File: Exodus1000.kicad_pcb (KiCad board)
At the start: 4 copper layers, 129.5 x 63.5 mm, 78 parts, among them J1 ARJ-169, J2 USB_B_Mini, J3 Conn_01x02, M1 ET60S-02-24-02-X-VP-GP, M2 ET60S-02-24-02-X-VP-GP, M3 ET60S-02-24-02-X-VP-GP, M4 ET60S-02-24-02-X-VP-GP, U1 TM4C1294NCPDTGOOD, U2 93LCxxB, U3 FT232H, U4 tusb2077a, U5 IS42S16400J-xT, Y1 Crystal_GND24, Y2 Crystal_GND24, Y3 Crystal_GND24

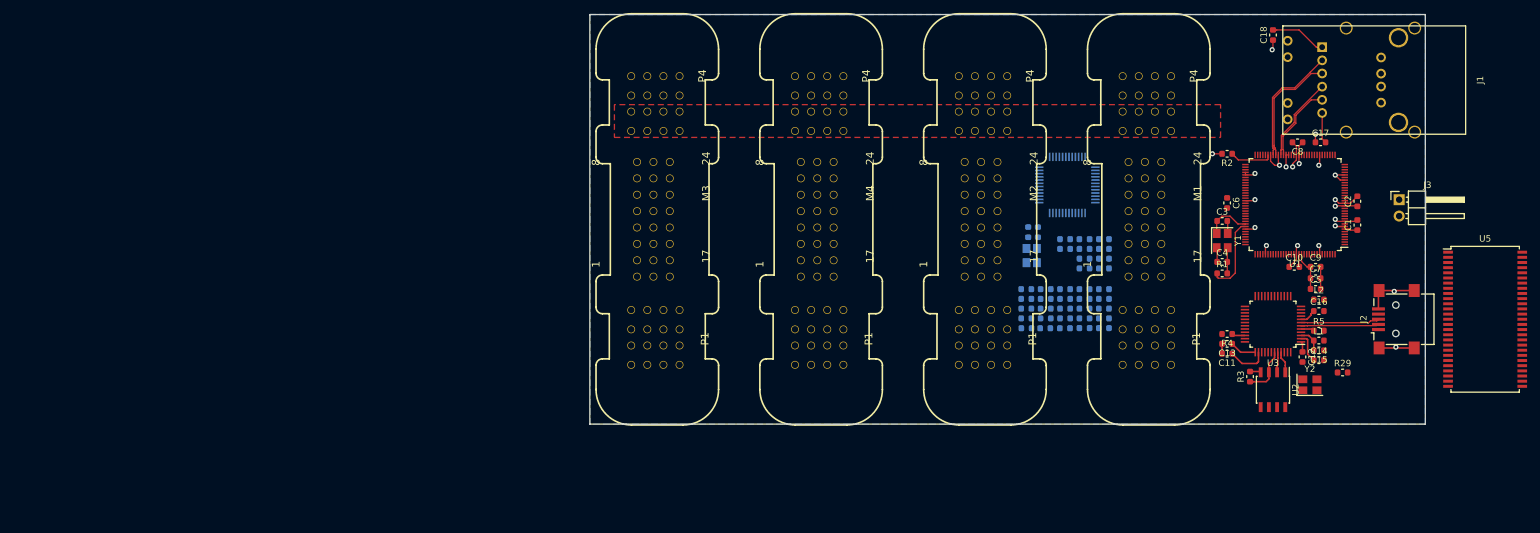
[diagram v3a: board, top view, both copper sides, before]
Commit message: schematics for expansion slots and memory
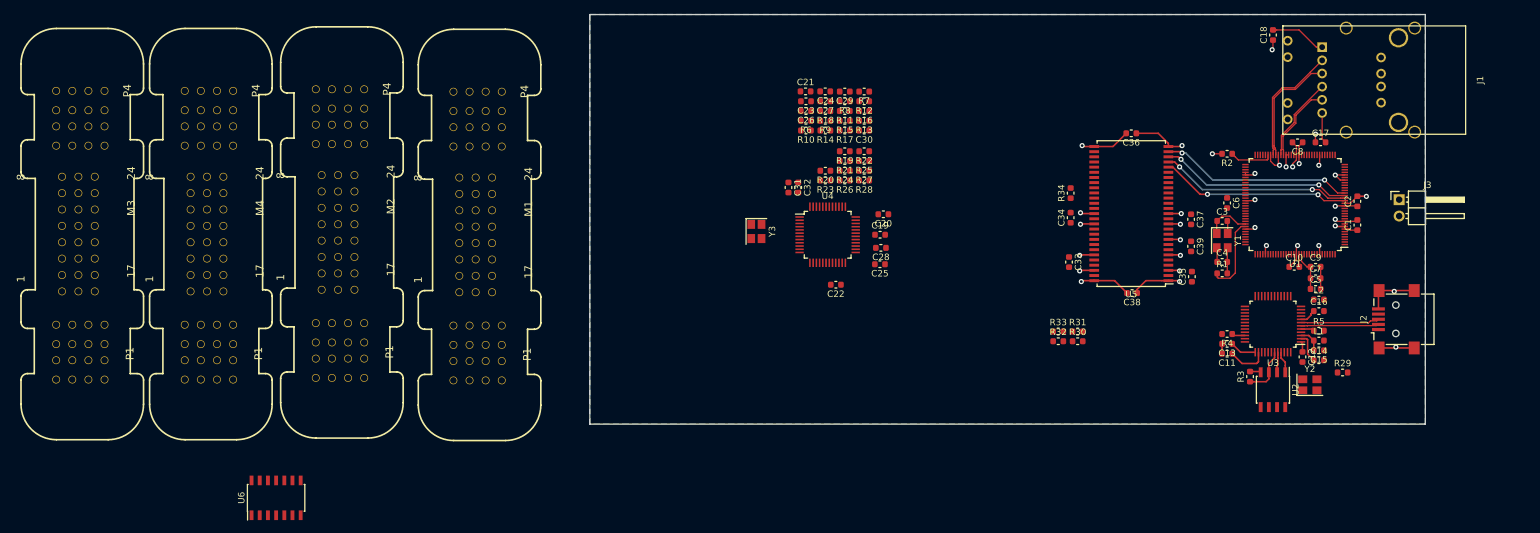
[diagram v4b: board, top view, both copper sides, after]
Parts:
- added C33: C_Small, Capacitor_SMD:C_0603_1608Metric, F.Cu at (134.0, 104.7)
- added C34: C_Small, Capacitor_SMD:C_0603_1608Metric, F.Cu at (134.2, 97.8)
- added C35: C_Small, Capacitor_SMD:C_0603_1608Metric, F.Cu at (153.0, 106.9)
- added C36: C_Small, Capacitor_SMD:C_0603_1608Metric, F.Cu at (143.6, 84.7)
- added C37: C_Small, Capacitor_SMD:C_0603_1608Metric, F.Cu at (152.9, 98.0)
- added C38: C_Small, Capacitor_SMD:C_0603_1608Metric, F.Cu at (143.8, 109.5)
- added C39: C_Small, Capacitor_SMD:C_0603_1608Metric, F.Cu at (152.9, 102.2)
- added R30: R_Small, Resistor_SMD:R_0603_1608Metric, F.Cu at (135.3, 116.9)
- added R31: R_Small, Resistor_SMD:R_0603_1608Metric, F.Cu at (135.3, 115.4)
- added R32: R_Small, Resistor_SMD:R_0603_1608Metric, F.Cu at (132.3, 116.9)
- added R33: R_Small, Resistor_SMD:R_0603_1608Metric, F.Cu at (132.3, 115.4)
- added R34: 0, Resistor_SMD:R_0603_1608Metric, F.Cu at (134.2, 94.0)
- added U6: 74LS125, Package_SO:SOIC-14_3.9x8.7mm_P1.27mm, F.Cu at (11.0, 141.2)
- C19, C20, C21, C22, C23, C24, C25, C26, C27, C28, C29, C30, C31, C32, R10, R11, R12, R13, R14, R15, R16, R17, R18, R19, R20, R21, R22, R23, R24, R25, R26, R27, R28, R6, R7, R8, R9, U4, Y3: moved to F.Cu
- U5: value IS42S16400J-xT -> IS42S16400J-xC
- moved M1 103.8 mm to (42.3, 100.5)
- moved M2 99.7 mm to (21.0, 100.1)
- moved M4 94.6 mm to (0.64, 100.3)
- moved M3 89.2 mm to (-19.3, 100.3)
- moved U5 57.3 mm to (143.6, 97.2), turned to 180 degrees
- moved C21 52.3 mm to (93.1, 78.2)
- moved C24 52.3 mm to (96.2, 78.2)
- moved R7 52.2 mm to (102.2, 78.2)
- moved C29 52.2 mm to (99.2, 78.2)
- moved C23 50.1 mm to (93.2, 79.7)
- moved R12 50.1 mm to (102.2, 79.7)
- moved C27 50.1 mm to (96.2, 79.7)
- moved R8 50.1 mm to (99.2, 79.7)
- moved C26 48.2 mm to (93.2, 81.3)
- moved R16 48.2 mm to (102.2, 81.3)
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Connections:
- net Net-(M3-Pad4) renamed /Connectors/JTAG_TD0
- C21 pad 1: Net-(C21-Pad1) -> /Connectors/sheet5C922FED/DP3
- C22 pad 1: Net-(C22-Pad1) -> /Connectors/sheet5C922FED/DM3
- C23 pad 1: Net-(C23-Pad1) -> /Connectors/sheet5C922FED/DP1
- C24 pad 1: Net-(C24-Pad1) -> /Connectors/sheet5C922FED/DM1
- C25 pad 1: Net-(C25-Pad1) -> /Connectors/sheet5C922FED/DP4
- C26 pad 1: Net-(C26-Pad1) -> /Connectors/sheet5C922FED/DM4
- C27 pad 1: Net-(C27-Pad1) -> /Connectors/sheet5C922FED/DP2
- C28 pad 1: Net-(C28-Pad1) -> /Connectors/sheet5C922FED/DP5
- C29 pad 1: Net-(C29-Pad1) -> /Connectors/sheet5C922FED/DM2
- C30 pad 1: Net-(C30-Pad1) -> /Connectors/sheet5C922FED/DM5
- J1 pad U2: Net-(J1-PadU2) -> /Connectors/D5_N
- J1 pad U3: Net-(J1-PadU3) -> /Connectors/D5_P
- M1 pad 1: Net-(M1-Pad1) -> /Connectors/D4_P
- M1 pad 10: Net-(M1-Pad10) -> /Connectors/BOARD_SENSE_4
- M1 pad 11: Net-(M1-Pad11) -> /Connectors/~SYSRESET
- M1 pad 2: Net-(M1-Pad2) -> /Connectors/D4_N
- M1 pad 3: Net-(M1-Pad3) -> /JTAG_TMS
- M1 pad 4: Net-(M1-Pad4) -> /Connectors/JTAG_TDO_3
- M1 pad 5: Net-(M1-Pad5) -> /JTAG_TDI
- M1 pad 6: Net-(M1-Pad6) -> /JTAG_TCK
- M1 pad 7: Net-(M1-Pad7) -> /Connectors/~JTAG_TRST
- M1 pad 8: Net-(M1-Pad8) -> /Connectors/~ENABLE
- M1 pad 9: Net-(M1-Pad9) -> /Connectors/~INHIBIT
- M2 pad 1: Net-(M2-Pad1) -> /Connectors/D3_P
- M2 pad 10: Net-(M2-Pad10) -> /Connectors/BOARD_SENSE_3
- M2 pad 11: Net-(M2-Pad11) -> /Connectors/~SYSRESET
- M2 pad 2: Net-(M2-Pad2) -> /Connectors/D3_N
- M2 pad 3: Net-(M2-Pad3) -> /JTAG_TMS
- M2 pad 4: Net-(M2-Pad4) -> /Connectors/JTAG_TDO_2
- M2 pad 5: Net-(M2-Pad5) -> /Connectors/JTAG_TDO_3
- M2 pad 6: Net-(M2-Pad6) -> /JTAG_TCK
- M2 pad 7: Net-(M2-Pad7) -> /Connectors/~JTAG_TRST
- M2 pad 8: Net-(M2-Pad8) -> /Connectors/~ENABLE
- M2 pad 9: Net-(M2-Pad9) -> /Connectors/~INHIBIT
- M3 pad 1: Net-(M3-Pad1) -> /Connectors/D1_P
- M3 pad 10: Net-(M3-Pad10) -> /Connectors/BOARD_SENSE_1
- M3 pad 11: Net-(M3-Pad11) -> /Connectors/~SYSRESET
- M3 pad 2: Net-(M3-Pad2) -> /Connectors/D1_N
- M3 pad 3: Net-(M3-Pad3) -> /JTAG_TMS
- M3 pad 5: Net-(M3-Pad5) -> /Connectors/JTAG_TDO_1
- M3 pad 6: Net-(M3-Pad6) -> /JTAG_TCK
- M3 pad 7: Net-(M3-Pad7) -> /Connectors/~JTAG_TRST
- M3 pad 8: Net-(M3-Pad8) -> /Connectors/~ENABLE
- M3 pad 9: Net-(M3-Pad9) -> /Connectors/~INHIBIT
- M4 pad 1: Net-(M4-Pad1) -> /Connectors/D2_P
- M4 pad 10: Net-(M4-Pad10) -> /Connectors/BOARD_SENSE_2
- M4 pad 11: Net-(M4-Pad11) -> /Connectors/~SYSRESET
- M4 pad 2: Net-(M4-Pad2) -> /Connectors/D2_N
- M4 pad 3: Net-(M4-Pad3) -> /JTAG_TMS
- M4 pad 4: Net-(M4-Pad4) -> /Connectors/JTAG_TDO_1
- M4 pad 5: Net-(M4-Pad5) -> /Connectors/JTAG_TDO_2
- M4 pad 6: Net-(M4-Pad6) -> /JTAG_TCK
- M4 pad 7: Net-(M4-Pad7) -> /Connectors/~JTAG_TRST
- M4 pad 8: Net-(M4-Pad8) -> /Connectors/~ENABLE
- M4 pad 9: Net-(M4-Pad9) -> /Connectors/~INHIBIT
- R10 pad 1: /Connectors/sheet5C922FED/D5_N -> /Connectors/D3_N
- R10 pad 2: Net-(C22-Pad1) -> /Connectors/sheet5C922FED/DM3
- R11 pad 1: /Connectors/sheet5C922FED/D5_P -> /Connectors/D1_P
- R11 pad 2: Net-(C23-Pad1) -> /Connectors/sheet5C922FED/DP1
- R12 pad 1: /Connectors/sheet5C922FED/D5_N -> /Connectors/D1_N
- R12 pad 2: Net-(C24-Pad1) -> /Connectors/sheet5C922FED/DM1
- R13 pad 1: /Connectors/sheet5C922FED/D5_P -> /Connectors/D4_P
- R13 pad 2: Net-(C25-Pad1) -> /Connectors/sheet5C922FED/DP4
- R14 pad 1: /Connectors/sheet5C922FED/D5_N -> /Connectors/D4_N
- R14 pad 2: Net-(C26-Pad1) -> /Connectors/sheet5C922FED/DM4
- R15 pad 1: /Connectors/sheet5C922FED/D5_P -> /Connectors/D2_P
- R15 pad 2: Net-(C27-Pad1) -> /Connectors/sheet5C922FED/DP2
- R16 pad 1: /Connectors/sheet5C922FED/D5_N -> /Connectors/D2_N
- R16 pad 2: Net-(C29-Pad1) -> /Connectors/sheet5C922FED/DM2
- R17 pad 1: /Connectors/sheet5C922FED/D5_P -> /Connectors/D5_P
- R17 pad 2: Net-(C28-Pad1) -> /Connectors/sheet5C922FED/DP5
- R18 pad 1: /Connectors/sheet5C922FED/D5_N -> /Connectors/D5_N
- R18 pad 2: Net-(C30-Pad1) -> /Connectors/sheet5C922FED/DM5
- R19 pad 2: /Connectors/sheet5C922FED/D5_P -> /Connectors/D3_P
- R20 pad 2: /Connectors/sheet5C922FED/D5_N -> /Connectors/D3_N
- R21 pad 2: /Connectors/sheet5C922FED/D5_P -> /Connectors/D1_P
- R22 pad 2: /Connectors/sheet5C922FED/D5_N -> /Connectors/D1_N
- R23 pad 2: /Connectors/sheet5C922FED/D5_P -> /Connectors/D4_P
- R24 pad 2: /Connectors/sheet5C922FED/D5_N -> /Connectors/D4_N
- R25 pad 2: /Connectors/sheet5C922FED/D5_P -> /Connectors/D2_P
- R26 pad 2: /Connectors/sheet5C922FED/D5_P -> /Connectors/D5_P
- R27 pad 2: /Connectors/sheet5C922FED/D5_N -> /Connectors/D2_N
- R28 pad 2: /Connectors/sheet5C922FED/D5_N -> /Connectors/D5_N
- R9 pad 1: /Connectors/sheet5C922FED/D5_P -> /Connectors/D3_P
- R9 pad 2: Net-(C21-Pad1) -> /Connectors/sheet5C922FED/DP3
- U1 pad 103: Net-(U1-Pad103) -> /Memory/EPIOS29
- U1 pad 104: Net-(U1-Pad104) -> /Memory/EPIOS30
- U1 pad 18: Net-(U1-Pad18) -> /Memory/EPIOS0
- U1 pad 19: Net-(U1-Pad19) -> /Memory/EPIOS1
- U1 pad 20: Net-(U1-Pad20) -> /Memory/EPIOS2
- U1 pad 21: Net-(U1-Pad21) -> /Memory/EPIOS3
- U1 pad 22: Net-(U1-Pad22) -> /Memory/EPIOS4
- U1 pad 23: Net-(U1-Pad23) -> /Memory/EPIOS5
- U1 pad 24: Net-(U1-Pad24) -> /Memory/EPIOS6
- U1 pad 25: Net-(U1-Pad25) -> /Memory/EPIOS7
- U1 pad 40: Net-(U1-Pad40) -> /Memory/EPIOS8
- U1 pad 41: Net-(U1-Pad41) -> /Memory/EPIOS9
- U1 pad 49: Net-(U1-Pad49) -> /Memory/EPIOS11
- U1 pad 50: Net-(U1-Pad50) -> /Memory/EPIOS10
- U1 pad 62: Net-(U1-Pad62) -> /Memory/EPIOS31
- U1 pad 75: Net-(U1-Pad75) -> /Memory/EPIOS12
- U1 pad 76: Net-(U1-Pad76) -> /Memory/EPIOS13
- U1 pad 77: Net-(U1-Pad77) -> /Memory/EPIOS14
- U1 pad 78: Net-(U1-Pad78) -> /Memory/EPIOS15
- U1 pad 81: Net-(U1-Pad81) -> /Memory/EPIOS16
- U1 pad 82: Net-(U1-Pad82) -> /Memory/EPIOS17
- U1 pad 83: Net-(U1-Pad83) -> /Memory/EPIOS18
- U1 pad 84: Net-(U1-Pad84) -> /Memory/EPIOS19
- U1 pad 92: Net-(U1-Pad92) -> /Memory/EPIOS28
- U3 pad 13: /Connectors/JTAG_TCK -> /JTAG_TCK
- U3 pad 14: /Connectors/JTAG_TDI -> /JTAG_TDI
- U3 pad 15: /Connectors/JTAG_TDO -> /JTAG_TDO
- U3 pad 16: /Connectors/JTAG_TMS -> /JTAG_TMS
- U4 pad 13: Net-(U4-Pad13) -> /Connectors/sheet5C922FED/DM1
- U4 pad 14: Net-(U4-Pad14) -> /Connectors/sheet5C922FED/DP1
- U4 pad 17: Net-(U4-Pad17) -> /Connectors/sheet5C922FED/DM2
- U4 pad 18: Net-(U4-Pad18) -> /Connectors/sheet5C922FED/DP2
- U4 pad 21: Net-(U4-Pad21) -> /Connectors/sheet5C922FED/DM3
- U4 pad 22: Net-(U4-Pad22) -> /Connectors/sheet5C922FED/DP3
- U4 pad 26: Net-(U4-Pad26) -> /Connectors/sheet5C922FED/DM4
- U4 pad 27: Net-(U4-Pad27) -> /Connectors/sheet5C922FED/DP4
- U4 pad 30: Net-(U4-Pad30) -> /Connectors/sheet5C922FED/DM5
- U4 pad 31: Net-(U4-Pad31) -> /Connectors/sheet5C922FED/DP5
- U5 pad 1: Net-(U5-Pad1) -> +3V3
- U5 pad 10: Net-(U5-Pad10) -> /Memory/EPIOS5
- U5 pad 11: Net-(U5-Pad11) -> /Memory/EPIOS6
- U5 pad 12: Net-(U5-Pad12) -> GND
- U5 pad 13: Net-(U5-Pad13) -> /Memory/EPIOS7
- U5 pad 14: Net-(U5-Pad14) -> +3V3
- U5 pad 15: Net-(U5-Pad15) -> /Memory/EPIOS16
- U5 pad 16: Net-(U5-Pad16) -> /Memory/EPIOS28
- U5 pad 17: Net-(U5-Pad17) -> /Memory/EPIOS18
- U5 pad 18: Net-(U5-Pad18) -> /Memory/EPIOS19
- U5 pad 19: Net-(U5-Pad19) -> /Memory/EPIOS29
- U5 pad 2: Net-(U5-Pad2) -> /Memory/EPIOS0
- U5 pad 20: Net-(U5-Pad20) -> /Memory/EPIOS13
- U5 pad 21: Net-(U5-Pad21) -> /Memory/EPIOS14
- U5 pad 22: Net-(U5-Pad22) -> /Memory/EPIOS10
- U5 pad 23: Net-(U5-Pad23) -> /Memory/EPIOS0
- U5 pad 24: Net-(U5-Pad24) -> /Memory/EPIOS1
- U5 pad 25: Net-(U5-Pad25) -> /Memory/EPIOS2
- U5 pad 26: Net-(U5-Pad26) -> /Memory/EPIOS3
- U5 pad 27: Net-(U5-Pad27) -> +3V3
- U5 pad 28: Net-(U5-Pad28) -> GND
- U5 pad 29: Net-(U5-Pad29) -> /Memory/EPIOS4
- U5 pad 3: Net-(U5-Pad3) -> +3V3
- U5 pad 30: Net-(U5-Pad30) -> /Memory/EPIOS5
- U5 pad 31: Net-(U5-Pad31) -> /Memory/EPIOS6
- U5 pad 32: Net-(U5-Pad32) -> /Memory/EPIOS7
- U5 pad 33: Net-(U5-Pad33) -> /Memory/EPIOS8
- U5 pad 34: Net-(U5-Pad34) -> /Memory/EPIOS9
- U5 pad 35: Net-(U5-Pad35) -> /Memory/EPIOS11
- U5 pad 36: Net-(U5-Pad36) -> /Memory/EPIOS12
- U5 pad 37: Net-(U5-Pad37) -> /Memory/EPIOS30
- U5 pad 39: Net-(U5-Pad39) -> /Memory/EPIOS17
- U5 pad 4: Net-(U5-Pad4) -> /Memory/EPIOS1
- U5 pad 41: Net-(U5-Pad41) -> GND
- U5 pad 42: Net-(U5-Pad42) -> /Memory/EPIOS8
- U5 pad 43: Net-(U5-Pad43) -> +3V3
- U5 pad 44: Net-(U5-Pad44) -> /Memory/EPIOS9
- U5 pad 45: Net-(U5-Pad45) -> /Memory/EPIOS10
- U5 pad 46: Net-(U5-Pad46) -> GND
- U5 pad 47: Net-(U5-Pad47) -> /Memory/EPIOS11
- U5 pad 48: Net-(U5-Pad48) -> /Memory/EPIOS12
- U5 pad 49: Net-(U5-Pad49) -> +3V3
- U5 pad 5: Net-(U5-Pad5) -> /Memory/EPIOS2
- U5 pad 50: Net-(U5-Pad50) -> /Memory/EPIOS13
- U5 pad 51: Net-(U5-Pad51) -> /Memory/EPIOS14
- U5 pad 52: Net-(U5-Pad52) -> GND
- U5 pad 53: Net-(U5-Pad53) -> /Memory/EPIOS15
- U5 pad 54: Net-(U5-Pad54) -> GND
- U5 pad 6: Net-(U5-Pad6) -> GND
- U5 pad 7: Net-(U5-Pad7) -> /Memory/EPIOS3
- U5 pad 8: Net-(U5-Pad8) -> /Memory/EPIOS4
- U5 pad 9: Net-(U5-Pad9) -> +3V3
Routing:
- net /Memory/EPIOS3: track 0.00 -> 30.0 mm, vias 0 -> 2
- net /Memory/EPIOS2: track 0.00 -> 29.8 mm, vias 0 -> 2
- net /Memory/EPIOS1: track 0.00 -> 29.7 mm, vias 0 -> 2
- net /Memory/EPIOS0: track 0.00 -> 29.5 mm, vias 0 -> 2
- net +3V3: track 30.3 -> 56.5 mm, vias 12 -> 19
- net GND: track 45.8 -> 69.5 mm, vias 9 -> 15
- removed copper zone on F.Cu, net +5V

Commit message: almost done with draft 1 of layout
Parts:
- added D1: LED, LED_SMD:LED_0603_1608Metric, F.Cu at (188.0, 88.4)
- added R35: R_Small, Resistor_SMD:R_0603_1608Metric, B.Cu at (114.3, 106.4)
- R31, R32, R33, U6: moved to B.Cu
- moved R34 149.1 mm to (279.7, 126.7), turned to 270 degrees
- moved M3 146.3 mm to (127.0, 98.4)
- moved M4 102.3 mm to (102.9, 98.4)
- moved U6 85.6 mm to (91.7, 112.5), turned to 180 degrees
- moved Y3 74.7 mm to (158.2, 117.1)
- moved C36 71.8 mm to (210.4, 111.1), turned to 90 degrees
- moved C32 71.5 mm to (158.2, 120.1), turned to 180 degrees
- moved C31 70.9 mm to (158.2, 114.0), turned to 0 degrees
- moved R18 70.7 mm to (151.1, 125.7), turned to 90 degrees
- moved R17 67.8 mm to (152.9, 125.7), turned to 90 degrees
- moved R6 67.2 mm to (154.2, 111.0), turned to 90 degrees
- moved R31 67.2 mm to (68.8, 105.9), turned to 270 degrees
- moved C21 66.8 mm to (142.7, 122.9), turned to 180 degrees
- moved C26 66.2 mm to (142.2, 125.7), turned to 270 degrees
- moved R26 65.6 mm to (153.9, 128.3)
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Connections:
- net Net-(C12-Pad1) renamed /Connectors/sheet5C96EC1B/OSC1
- net Net-(C14-Pad1) renamed /Connectors/sheet5C96EC1B/OSC0_R
- net Net-(R34-Pad1) renamed /Memory/CLK
- net Net-(R4-Pad1) renamed /Connectors/sheet5C96EC1B/OSC0
- net Net-(R6-Pad1) renamed /Connectors/sheet5C922FED/DP0
- net Net-(R7-Pad1) renamed /Connectors/sheet5C922FED/DM0
- M1 pad 1: /Connectors/D4_P -> /Connectors/D4_N
- M1 pad 16: Net-(M1-Pad16) -> /Connectors/~INHIBIT
- M1 pad 2: /Connectors/D4_N -> /Connectors/D4_P
- M1 pad 5: /JTAG_TDI -> /Connectors/JTAG_TDO_4
- M1 pad 9: /Connectors/~INHIBIT -> Net-(M1-Pad9)
- M2 pad 1: /Connectors/D3_P -> /Connectors/D3_N
- M2 pad 16: Net-(M2-Pad16) -> /Connectors/~INHIBIT
- M2 pad 2: /Connectors/D3_N -> /Connectors/D3_P
- M2 pad 9: /Connectors/~INHIBIT -> Net-(M2-Pad9)
- M3 pad 1: /Connectors/D1_P -> /Connectors/D1_N
- M3 pad 16: Net-(M3-Pad16) -> /Connectors/~INHIBIT
- M3 pad 2: /Connectors/D1_N -> /Connectors/D1_P
- M3 pad 4: /Connectors/JTAG_TD0 -> /JTAG_TDO
- M3 pad 9: /Connectors/~INHIBIT -> Net-(M3-Pad9)
- M4 pad 1: /Connectors/D2_P -> /Connectors/D2_N
- M4 pad 16: Net-(M4-Pad16) -> /Connectors/~INHIBIT
- M4 pad 2: /Connectors/D2_N -> /Connectors/D2_P
- M4 pad 9: /Connectors/~INHIBIT -> Net-(M4-Pad9)
- R30 pad 1: /Connectors/BOARD_SENSE_1 -> GND
- R30 pad 2: GND -> Net-(D1-Pad1)
- R31 pad 1: /Connectors/BOARD_SENSE_2 -> /Connectors/BOARD_SENSE_4
- R33 pad 1: /Connectors/BOARD_SENSE_4 -> /Connectors/BOARD_SENSE_1
- U3 pad 14: /JTAG_TDI -> /Connectors/JTAG_TDO_4
- U3 pad 15: /JTAG_TDO -> /JTAG_TDI
- U6 pad 11: /JTAG_TDI -> /Connectors/JTAG_TDO_4
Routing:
- net /Connectors/JTAG_TDO_4: track 0.00 -> 174.5 mm, vias 0 -> 2
- net /Connectors/D4_P: track 0.00 -> 124.5 mm
- net /Connectors/D4_N: track 0.00 -> 121.1 mm
- net /Connectors/~JTAG_TRST: track 0.00 -> 104.5 mm
- net /JTAG_TCK: track 0.00 -> 103.6 mm
- net /JTAG_TMS: track 0.00 -> 99.0 mm
- net /Connectors/D3_P: track 0.00 -> 97.8 mm
- net /Connectors/D3_N: track 0.00 -> 96.1 mm
- net GND: track 69.5 -> 151.6 mm, vias 15 -> 44
- net /JTAG_TDO: track 0.00 -> 81.8 mm, vias 0 -> 1
- net /Connectors/D2_P: track 0.00 -> 80.7 mm
- net /Connectors/D2_N: track 0.00 -> 79.1 mm
- net /Connectors/D5_P: track 0.00 -> 76.4 mm
- net /Connectors/D5_N: track 0.00 -> 74.9 mm
- net /Connectors/~ENABLE: track 0.00 -> 72.7 mm
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- added copper zone on F.Cu, net +5V
- added copper zone on In2.Cu, net +BATT
- added copper zone on In1.Cu, net GND
- removed copper zone on In1.Cu, net +BATT
- removed copper zone on In2.Cu, net GND
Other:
- board size 129.5 x 63.5 mm -> 147.3 x 64.5 mm

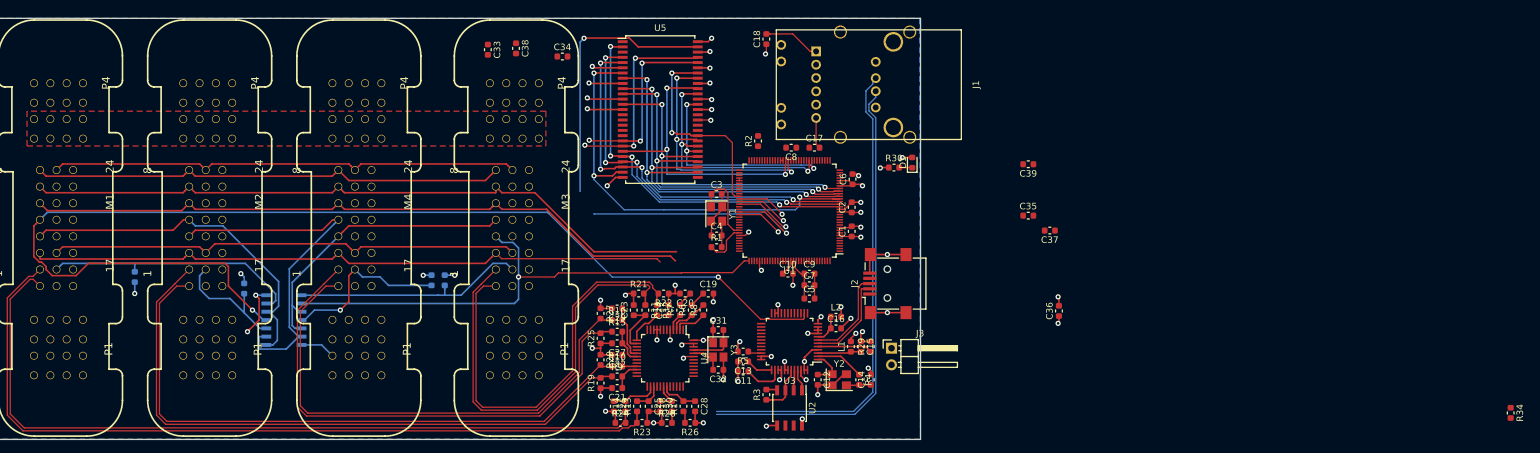
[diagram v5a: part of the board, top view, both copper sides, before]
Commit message: finished the ram ic routing
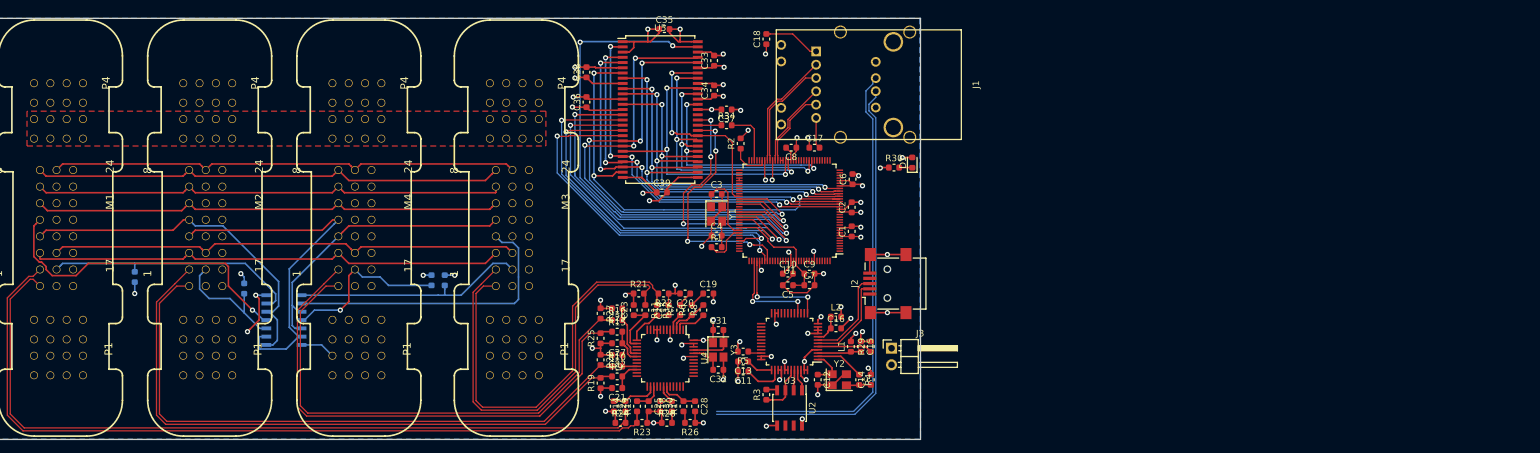
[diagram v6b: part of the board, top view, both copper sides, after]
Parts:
- moved R34 128.0 mm to (159.5, 82.7), turned to 0 degrees
- moved C36 79.1 mm to (138.0, 79.1)
- moved C35 62.6 mm to (150.0, 67.9)
- moved C39 56.3 mm to (149.6, 93.0), turned to 0 degrees
- moved C37 52.9 mm to (159.5, 80.3)
- moved C33 34.7 mm to (157.6, 72.8), turned to 90 degrees
- moved C34 23.8 mm to (157.6, 77.3), turned to 90 degrees
- moved C38 11.4 mm to (138.0, 74.5), turned to 90 degrees
- moved C5 3.88 mm to (168.9, 107.2), turned to 180 degrees
- moved R2 2.69 mm to (161.7, 85.5)
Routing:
- net /Connectors/JTAG_TDO_4: track 174.5 -> 49.2 mm, vias 2 -> 1
- net /Memory/EPIOS18: track 0.00 -> 59.3 mm, vias 0 -> 2
- net /Memory/EPIOS19: track 0.00 -> 57.4 mm, vias 0 -> 2
- net /Memory/EPIOS29: track 0.00 -> 54.4 mm, vias 0 -> 2
- net /Memory/EPIOS16: track 13.7 -> 61.5 mm, vias 1 -> 2
- net GND: track 151.6 -> 197.5 mm, vias 44 -> 49
- net /Memory/EPIOS14: track 38.7 -> 76.9 mm
- net /Memory/EPIOS13: track 36.1 -> 73.8 mm
- net /Memory/EPIOS17: track 9.08 -> 46.1 mm, vias 2 -> 4
- net /Memory/EPIOS30: track 0.00 -> 36.4 mm, vias 0 -> 4
- net /JTAG_TDO: track 81.8 -> 45.6 mm, vias 1 -> 0
- net +3V3: track 62.9 -> 96.4 mm, vias 22 -> 25
- net /Memory/EPIOS15: track 50.3 -> 82.4 mm, vias 2 -> 3
- net /Connectors/~JTAG_TRST: track 104.5 -> 72.7 mm
- net /Memory/EPIOS28: track 25.6 -> 56.0 mm, vias 0 -> 2
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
